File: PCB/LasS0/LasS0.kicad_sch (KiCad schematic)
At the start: 38 parts, among them J1 CiKe2PinSock, J1_1 CiKe2PinPlug, J2 CiKe2PinSock, J2_1 CiKe2PinPlug, J3 CiKe2PinSock, J3_1 CiKe2PinPlug, J4 CiKe2PinSock, J4_1 CiKe2PinPlug

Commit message: Start PCB, add mechanicals
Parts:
- added H1, H2: MountingHole, MeineBib:EigenesMountingHole_2.7mm_M2.5, symbol Mechanical:MountingHole
- added LOGO1: Binary-6, MeineBib:Binary_6_v0.1, symbol Mechanical:MountingHole
- added LOGO3: OSHW, Symbol:OSHW-Symbol_6.7x6mm_SilkScreen, symbol Mechanical:MountingHole
- gave numbers to parts that had none: 26
- renumbered JP1_A to JP1_A1, JP1_B to JP1_B1, JP2_A to JP2_A1, JP2_B to JP2_B1
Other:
- title: (none) -> LasS0

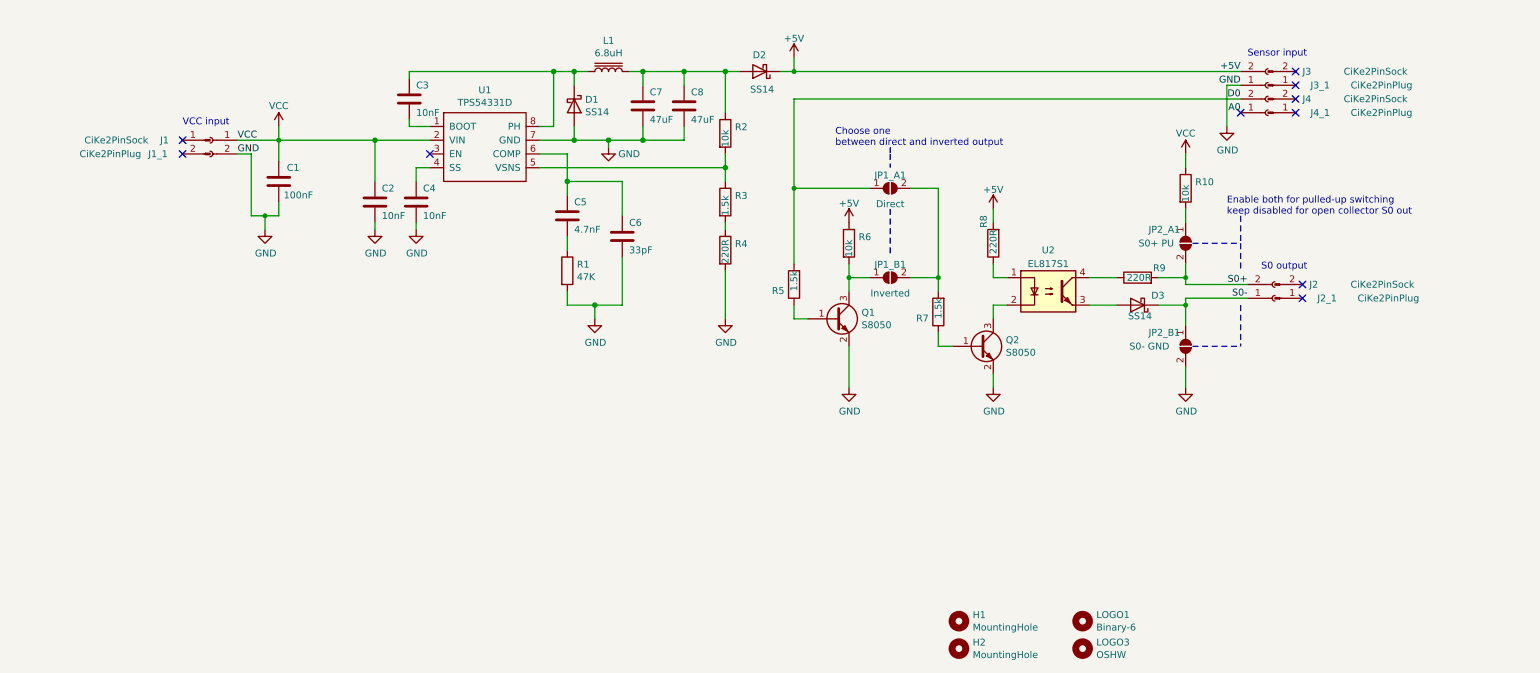
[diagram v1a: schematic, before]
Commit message: Update PCB:
- Switch to MOSFET input stage
- Add optional pullups/pulldowns on DO input
- Sadly make LOGO less pretty

Fabrication files are NOT updated yet, PCB version number is NOT updated yet
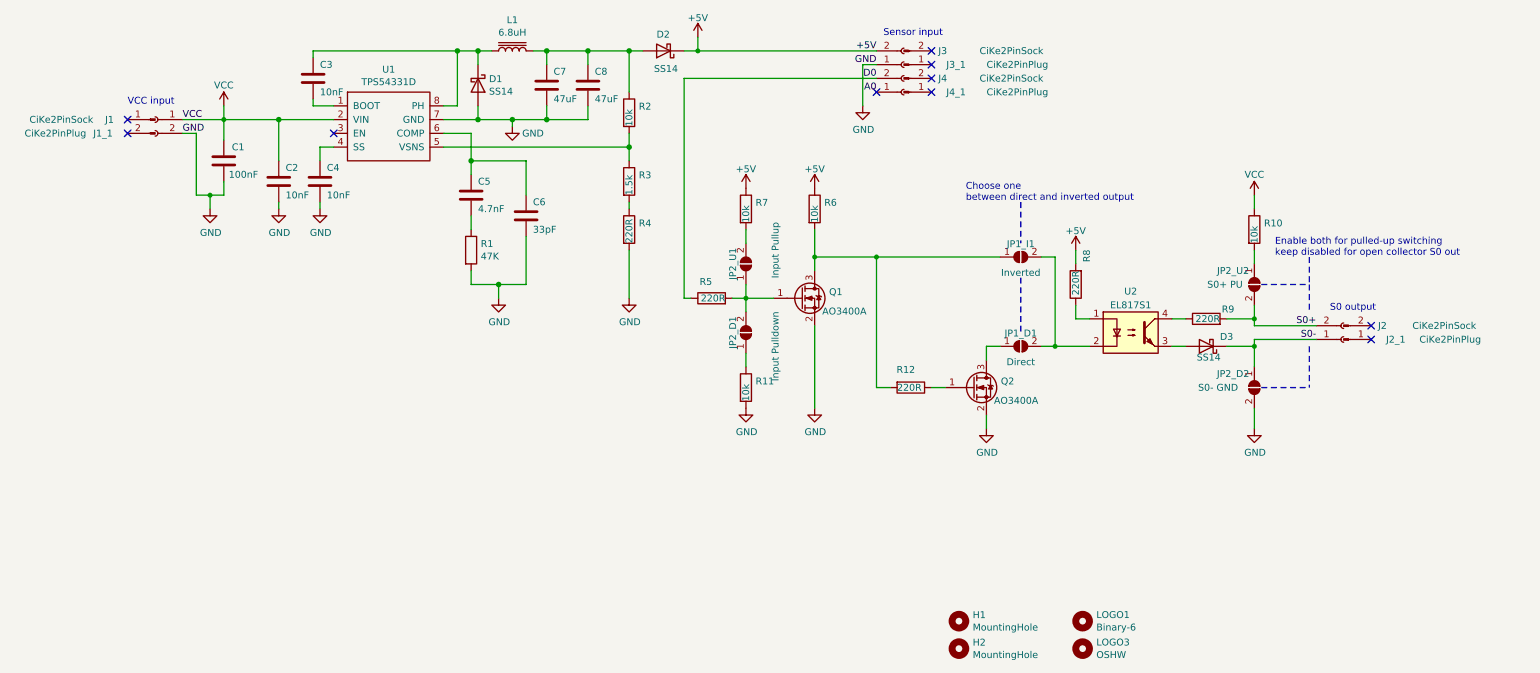
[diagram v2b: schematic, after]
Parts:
- removed Q1, Q2: S8050, Package_TO_SOT_SMD:SOT-23, symbol MeineBibli:S8050_correctpins
- added JP2_D1: Input Pulldown, Jumper:SolderJumper-2_P1.3mm_Open_TrianglePad1.0x1.5mm, symbol Jumper:SolderJumper_2_Open
- added JP2_U1: Input Pullup, Jumper:SolderJumper-2_P1.3mm_Open_TrianglePad1.0x1.5mm, symbol Jumper:SolderJumper_2_Open
- added Q1, Q2: AO3400A, Package_TO_SOT_SMD:SOT-23, symbol Transistor_FET:AO3400A
- added R11: 10k, Resistor_SMD:R_0603_1608Metric, symbol Device:R
- added R12: 220R, Resistor_SMD:R_0603_1608Metric, symbol Device:R
- R5: value 1.5k -> 220R; LCSC C22843 -> C22962
- R7: value 1.5k -> 10k; LCSC C22843 -> C25804
- renumbered JP1_A1 to JP1_D1, JP1_B1 to JP1_I1, JP2_B1 to JP2_D2, JP2_A1 to JP2_U2
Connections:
- net +5V: now also R7.1
- net D0: now also R5.1; no longer JP1_D1.1 (A), R5.2
- net GND: now also Q1.2 (S), Q2.2 (S), R11.2
- net at U2.2: now also JP1_D1.2 (B), JP1_I1.2 (B)
- net at JP1_I1.1 (A), R6.2: now also Q1.3 (D), R12.2
- new net: JP1_D1.1 (A), Q2.3 (D)
- new net: JP2_U1.2 (B), R7.2
- new net: JP2_D1.2 (B), JP2_U1.1 (A), Q1.1 (G), R5.2
- new net: JP2_D1.1 (A), R11.1
- new net: Q2.1 (G), R12.1
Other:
- moved on the sheet: C1, C2, C3, C4, C5, C6, C7, C8, D1, D2, D3, J1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
